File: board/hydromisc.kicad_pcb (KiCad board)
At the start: 2 copper layers, 100 x 100 mm, 174 parts, among them CN1 DC_COAX_POWER_NO_SHIELD, CN10 MOLEX_2x1, CN11 MOLEX_2x1, CN12 MOLEX_2x3, CN13 MOLEX_2x3, CN14 COAX_CONNECTOR, CN15 HEADER_6, CN16 MOLEX_2x2, CN2 MOLEX_2x1, CN3 COAX_CONNECTOR, CN4 MOLEX_2x2, CN5 MOLEX_2x4, CN6 MOLEX_2x5, CN7 MOLEX_2x1, CN8 MOLEX_2x1, CN9 MOLEX_2x1, IC1 LM2596, IC2 74HC594, IC3 LM2596, IC4 74HC594, IC5 opamp, IC6 vref-diode, IC7 AZ1117I-LDO, Q1 NFET, Q10 NFET, Q11 NFET, Q12 NFET, Q13 NFET, Q14 NFET, Q15 NFET, Q16 NFET, Q17 NFET, Q18 NFET, Q19 NFET, Q2 NFET, Q20 NFET, Q21 NFET, Q22 NFET, Q23 NFET, Q24 NFET, Q25 NFET, Q3 NFET, Q4 NFET, Q5 NFET, Q6 NFET, Q7 NFET, Q8 NFET, Q9 NFET, U1 ESP32-WROOM-32E

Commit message: Update PCB to rev B.
Add the missing pull-up on ESP32_EN, some pull-down on Vuser to
fight off-brand LM2596 leakage current, and a README.md explaining.
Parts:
- added R54: 10k, hydromisc:HM_0603, F.Cu at (173.9, 113.3)
- added R55: 1k, hydromisc:HM_0603, F.Cu at (113.4, 109.9)
- added R56: 1k, hydromisc:HM_0603, F.Cu at (117.7, 109.9)
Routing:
- net ESP32_EN: track 34.7 -> 51.9 mm, vias 2 -> 3
- net Vuser: track 176.4 -> 182.5 mm
- net Net-(R55-Pad2): track 0.00 -> 2.80 mm
- net GND: track 1019.4 -> 1021.6 mm
- net +3V3: track 339.2 -> 341.1 mm
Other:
- board text added: "07/2021"
- board text added: "hydromisc rev B"
- board text removed: "03/2021"
- board text removed: "hydromisc rev A"

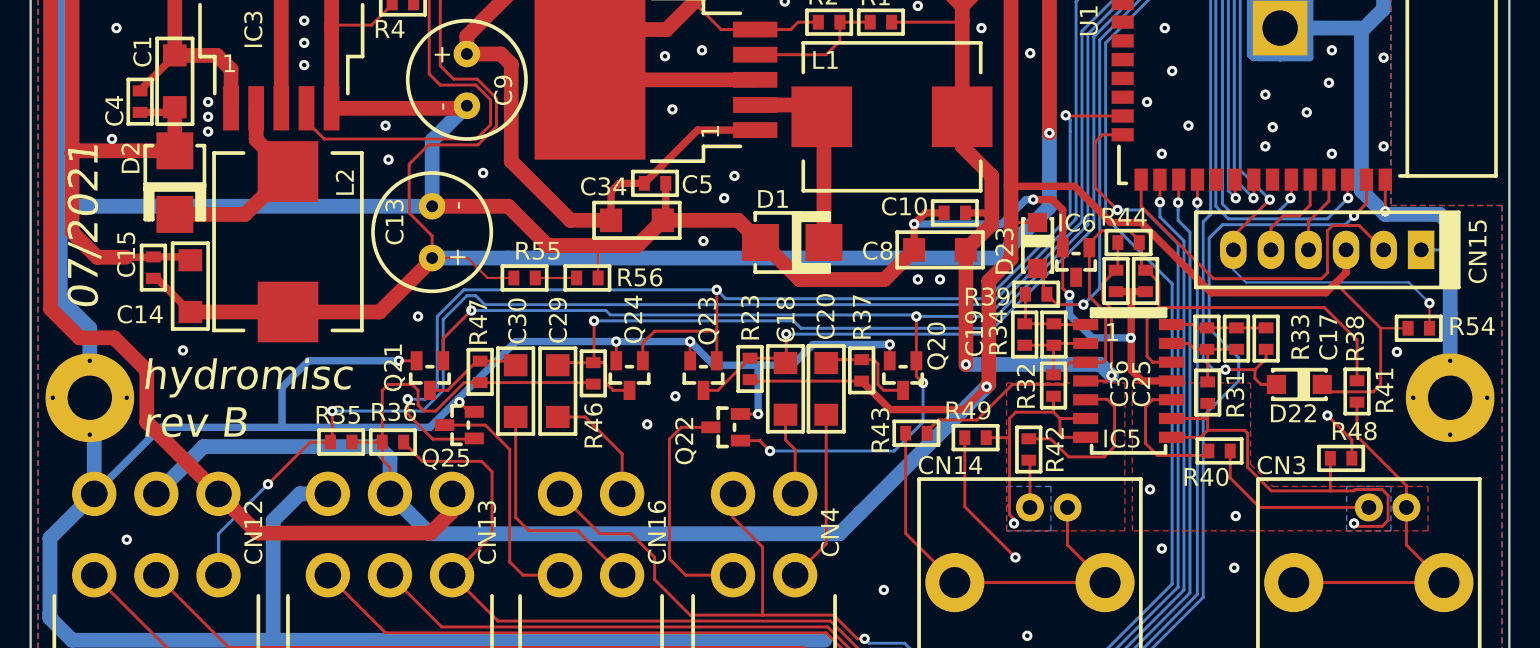
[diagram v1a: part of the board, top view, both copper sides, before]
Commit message: Add capacitors directly across pH probes.
This fixes a problem with 60 Hz (or 50 Hz) pickup, when the wires are
long or the noise is coupling to the water. Also replace the 1k resistors
to the shield with zero-ohm resistors, to further reduce that noise.

This updates the board to rev C. Also check in PDF schematics, BOM,
and Gerbers.
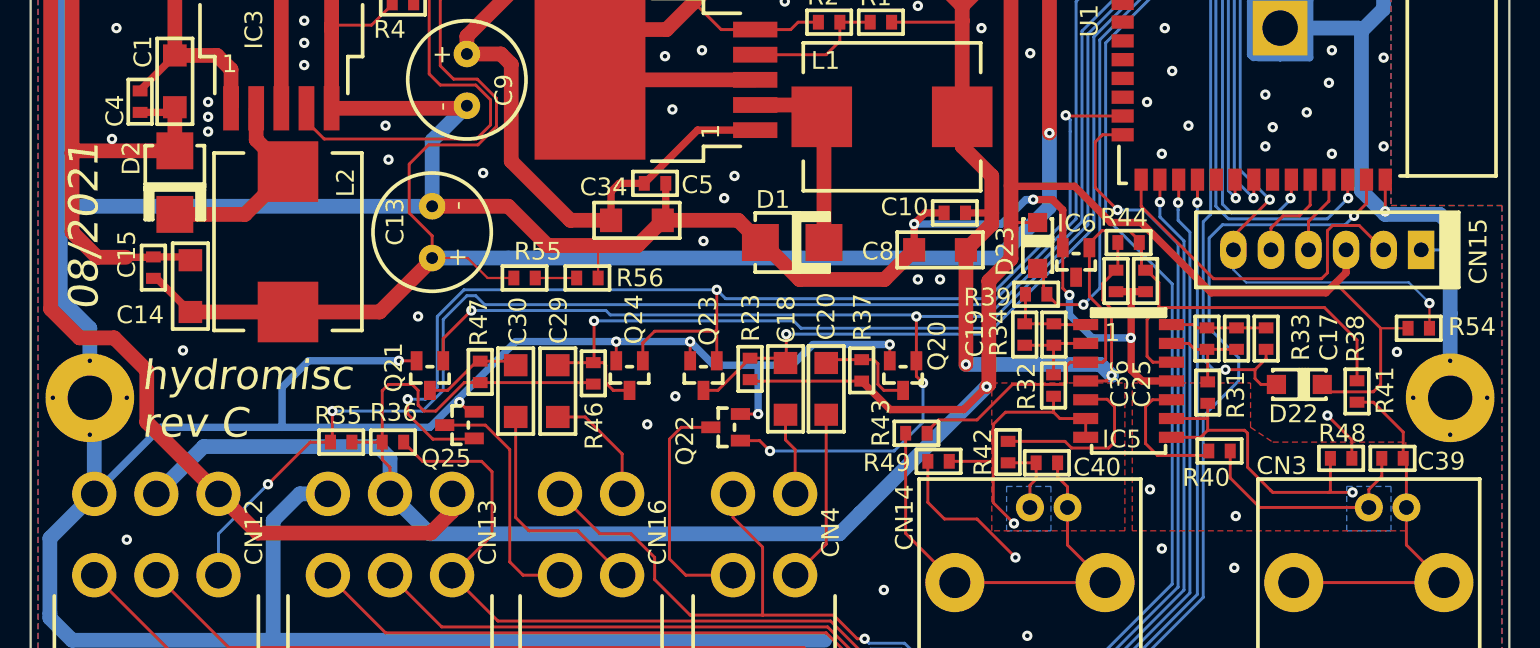
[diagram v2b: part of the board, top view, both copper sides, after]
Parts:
- added C39: 100n, hydromisc:HM_0603, F.Cu at (172.1, 122.1)
- added C40: 100n, hydromisc:HM_0603, F.Cu at (148.7, 122.4)
- R41, R43: value 1k -> zerohm
- moved R49 2.97 mm to (141.4, 122.3)
- moved R42 1.41 mm to (146.1, 121.7)
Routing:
- net PH_0_SHIELD: track 28.8 -> 22.2 mm
- net Net-(C39-Pad1): track 12.0 -> 15.7 mm
- net Net-(C40-Pad2): track 27.8 -> 31.3 mm
- net Net-(C40-Pad1): track 3.23 -> 5.09 mm
- net PH_1_SHIELD: track 18.4 -> 19.4 mm
- net GND: track 1021.6 -> 1022.4 mm
- net Net-(IC5-Pad5): track 11.5 -> 12.1 mm
- net Net-(C39-Pad2): track 24.8 -> 25.4 mm
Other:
- board text added: "08/2021"
- board text added: "hydromisc rev C"
- board text removed: "07/2021"
- board text removed: "hydromisc rev B"
